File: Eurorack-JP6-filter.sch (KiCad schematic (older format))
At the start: 79 parts

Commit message: schematic capture almost finished
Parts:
- removed C?: C_US, symbol C_US
- removed R?: R_US, symbol R_US
- removed U?: LM13700, symbol LM13700
- removed U?: DG408, symbol DG408
- removed VR?: POT_US, symbol POT_US
- added C?: 33pF, symbol C_US
- added C? (x2): 330pF, symbol C_US
- added C?: 4.7pF, symbol C_US
- added C?: 22pF, symbol C_US
- added C? (x2): 10μF, symbol CP_US
- added C?: 0.47μ, symbol C_US
- added D? (x2): 1N914, symbol D
- added D? (x4): LED, symbol LED
- added J?: JACK_MONO_SW, symbol JACK_MONO_SW
- added P?: CONN_02X05, symbol CONN_02X05
- added Q? (x2): J112, symbol Q_NJFET_DGS
- added R? (x5): 100K, symbol R_US
- added R? (x3): 68K, symbol R_US
- added R? (x3): 560, symbol R_US
- added R? (x3): 18K, symbol R_US
- added R? (x4): 33K, symbol R_US
- added R? (x5): 10K, symbol R_US
- added R?: 47K, symbol R_US
- added R?: 1K, symbol R_US
- added R? (x2): 10, symbol R_US
- added SW?: TACT_SWITCH, symbol TACT_SWITCH
- added U? (x3): LM13700, symbol LM13700
- added U? (x2): TL072-, symbol TL072-
- added U?: 40106, symbol 40106
- added U?: DG409, symbol DG409
- added U? (x2): CD4027, symbol CD4027
- C?: value CP_US -> 10μF
- C?: value 47pF -> 4.7pF
- R?: value R_US -> 200K
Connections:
- net labels added: IN1, IN2, OUT2A, OUT2B, OUT4, SW1, SW2
- wire segments 139 -> 297
- no-connect marks 6 -> 15
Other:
- moved on the sheet: C?, J?, Q?, R?, U?, U?A, U?B, VR?

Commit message: schematic capture almost done. Power on Reset circuit breadboarded and implemented in schematic
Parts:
- removed U?: 40106, symbol 40106
- added C?: 0.47μ, symbol C_US
- added D?: 1N914, symbol D
- added J?: JACK_MONO_SW, symbol JACK_MONO_SW
- added R? (x2): 330, symbol R_US
- added R?: 33K, symbol R_US
- added R?: 100K, symbol R_US
- added U? (x6): CD40106, symbol CD40106
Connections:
- net +12V: now also D?.1 (K), R?.2, U?.14 (VDD)
- net GND: now also U?.13 (X), C?.2, J?.1, U?.11 (In), U?.13 (In), U?.5 (In), U?.7 (VSS), U?.9 (In); no longer U?.12 (Cd), U?.4 (Cd)
- net at R?.1, R?.1, R?.1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: now also R?.1
- net at C?.1, R?.1: now also R?.1, U?.1 (In); no longer SW?.1
- net at U?.3 (Cp): now also U?.2 (Out)
- new net: R?.2, SW?.1
- new net: U?.12 (Cd), U?.4 (Cd), U?.4 (Out)
- new net: C?.1, D?.2 (A), R?.1, R?.2
- new net: R?.1, U?.3 (In)
- new net: J?.3, R?.2
- no-connect marks 15 -> 19
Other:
- note added: "00 LOW PASS 24 dB\n01 LOW PASS 12 dB\n10 BAND PASS 12 dB\n11 HIGH PASS 24 dB"
- note added: "POWER ON RESET"
- note added: "SWITCH DEBOUNCE"
- moved on the sheet: C?, J?, Q?, R?, SW?, U?A, U?B, VR?

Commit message: capture done, still need to doublecheck and annotate, then do footprint association
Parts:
- added C? (x8): 100n, symbol C_US
- gave numbers to parts that had none: 7
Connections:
- net +12V: now also U4.8 (V+), U5.11 (V+), U6.11 (V+), U7.11 (V+), C?.1, C?.1, C?.1, C?.1
- net -12V: now also U4.4 (V-), U5.6 (V-), U6.6 (V-), U7.6 (V-), C?.2, C?.2, C?.2, C?.2
- net GND: now also U5.14 (+), U6.14 (+), U7.14 (+), C?.1, C?.1, C?.1, C?.1, C?.2, C?.2, C?.2, C?.2; no longer U5.3 (+), U6.3 (+), U7.3 (+)
- net at R?.1: now also U5.16; no longer U5.1
- net at R?.1, R?.2: now also U5.13 (-); no longer U5.4 (-)
- net at C?.1, Q?.2 (G): now also U5.12; no longer U5.5
- net at C?.2, R?.1, R?.2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: now also U6.12; no longer U6.5
- net at R?.1: now also U7.16; no longer U7.1
- net at R?.1, R?.2: now also U7.13 (-); no longer U7.4 (-)
- net at C?.1, Q?.2 (G): now also U7.12; no longer U7.5
- net at R?.1: now also U6.16; no longer U6.1
- net at R?.1, R?.2: now also U6.13 (-); no longer U6.4 (-)
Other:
- note added: "DECOUPLING"
- moved on the sheet: C?, R?

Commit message: annotation done, export netlist and start footprint assignment
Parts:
- added TP1, TP2: TEST_POINT, symbol TEST_POINT
- SW1: renamed from SW?; value TACT_SWITCH -> KS-01Q
- VR1, VR2, VR3, VR4, VR6: renamed from VR?; value POT_US -> 50K
- VR5: renamed from VR?; value POT_US -> 100K
- gave numbers to parts that had none: 122
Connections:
- net at Q2.1 (E1), Q2.4 (E2): now also R27.1
- net at Q2.5 (B2), R17.2, R23.2: now also R25.2, TP2.1
- net at Q1.1 (E1), Q1.4 (E2): now also R20.1
- net at Q1.5 (B2), R11.1, R12.1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: now also R15.1, TP1.1
- net IN1 renamed SUM1
- net IN2 renamed SUM2
- net SW1 renamed SWX1
- net SW2 renamed SWY2
- no-connect marks 19 -> 21
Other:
- note added: "GROUND UNUSED\nCMOS INPUTS"
- note added: "LOG"
- note added: "RESET FLIP FLOPS TO\n '00' ON POWER UP"
- moved on the sheet: U11C, U11D, U11E, U11F

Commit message: footprints assigned, about to start layout
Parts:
- removed Q3, Q4, Q5, Q6: J112, symbol Q_NJFET_DGS
- added Q3, Q4, Q5, Q6: J112, MyModules:SOT23-JRL, symbol Q_NJFET_SDG
- C1, C11, C12, C13, C14, C15, C16, C17, C18, C19, C2, C20, C21, C22, C25, C3, C4, C5, C6, C7, C8, C9: footprint (none) -> MyModules:SM0603-C-JRL
- C10, C23, C24, R19: footprint (none) -> MyModules:2MM-POL-CAP
- D1, D2, D3, D4: footprint (none) -> MyModules:3MM-LED
- D5, D6, D7: footprint (none) -> MyModules:SOD323-JRL
- J1, J2, J3, J4, J5, J6: footprint (none) -> MyModules:PJ-301B-JACK
- P1: footprint (none) -> Pin_Headers:Pin_Header_Straight_2x05
- Q1, Q2: footprint (none) -> synth:SOT363-JRL
- R1, R11, R12, R13, R14, R15, R16, R17, R18, R2, R20, R21, R22, R23, R24, R25, R26, R27, R28, R29, R3, R30, R31, R32, R33, R34, R35, R36, R37, R38, R39, R4, R40, R41, R42, R43, R44, R45, R46, R47, R48, R49, R5, R50, R51, R52, R53, R54, R55, R56, R57, R58, R59, R6, R60, R61, R62, R63, R64, R65, R66, R67, R68, R69, R7, R70, R71, R72, R8, R9: footprint (none) -> MyModules:SM0603-R-JRL
- R10: value R_US -> 680K; footprint (none) -> MyModules:SM0603-R-JRL
- SW1: footprint (none) -> synth:KS-01Q-02-JRL
- TP1, TP2: footprint (none) -> MyModules:TEST POINT
- U1, U2, U3, U4: footprint (none) -> MyModules:TSSOP8-JRL
- U10, U9: footprint (none) -> Housings_SSOP:TSSOP-16_4.4x5mm_Pitch0.65mm
- U11: footprint (none) -> Housings_SSOP:TSSOP-14_4.4x5mm_Pitch0.65mm
- U5, U6, U7, U8: footprint (none) -> synth:SO16-JRL
- VR1, VR2, VR3, VR4: footprint (none) -> synth:RV16A-41-JRL
- VR5, VR7: footprint (none) -> MyModules:Bourns_3362P
- VR6: footprint (none) -> synth:RD901F-ALPHA-POT
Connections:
- net +12V: now also Q3.2 (D), Q4.2 (D), Q5.2 (D), Q6.2 (D)
- net at C6.1, U5.5: now also Q3.3 (G)
- net at R33.2, R35.2, R37.2: now also Q3.1 (S)
- net at C7.1, U5.12: now also Q4.3 (G)
- net at C3.1, R24.2, R40.2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: now also Q4.1 (S)
- net at C18.1, U7.5: now also Q5.3 (G)
- net at R50.1, R57.2, R60.2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: now also Q5.1 (S)
- net at C25.1, U7.12: now also Q6.3 (G)
- net at C8.1, R45.2, R69.2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: now also Q6.1 (S)

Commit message: placing components, a few footprints updated
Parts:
- R66, R67: footprint MyModules:SM0603-R-JRL -> MyModules:SM0805-HAND
- VR6: footprint synth:RD901F-ALPHA-POT -> synth:RV16A-41-JRL
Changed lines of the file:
@@
 F 0 "VR6" H 2350 10600 50  0000 C CNN
 F 1 "50K" H 2350 10670 50  0000 C CNN
-F 2 "synth:RD901F-ALPHA-POT" H 2350 10750 60  0001 C CNN
+F 2 "synth:RV16A-41-JRL" H 2350 10750 60  0001 C CNN
 F 3 "" H 2350 10750 60  0000 C CNN
 	1    2350 10750
@@
 F 0 "R66" V 18680 1400 50  0000 C CNN
 F 1 "10" V 18520 1400 50  0000 C CNN
-F 2 "MyModules:SM0603-R-JRL" H 18600 1400 60  0001 C CNN
+F 2 "MyModules:SM0805-HAND" H 18600 1400 60  0001 C CNN
 F 3 "" H 18600 1400 60  0000 C CNN
 	1    18600 1400
@@
 F 0 "R67" V 18680 2300 50  0000 C CNN
 F 1 "10" V 18520 2300 50  0000 C CNN
-F 2 "MyModules:SM0603-R-JRL" H 18600 2300 60  0001 C CNN
+F 2 "MyModules:SM0805-HAND" H 18600 2300 60  0001 C CNN
 F 3 "" H 18600 2300 60  0000 C CNN
 	1    18600 2300

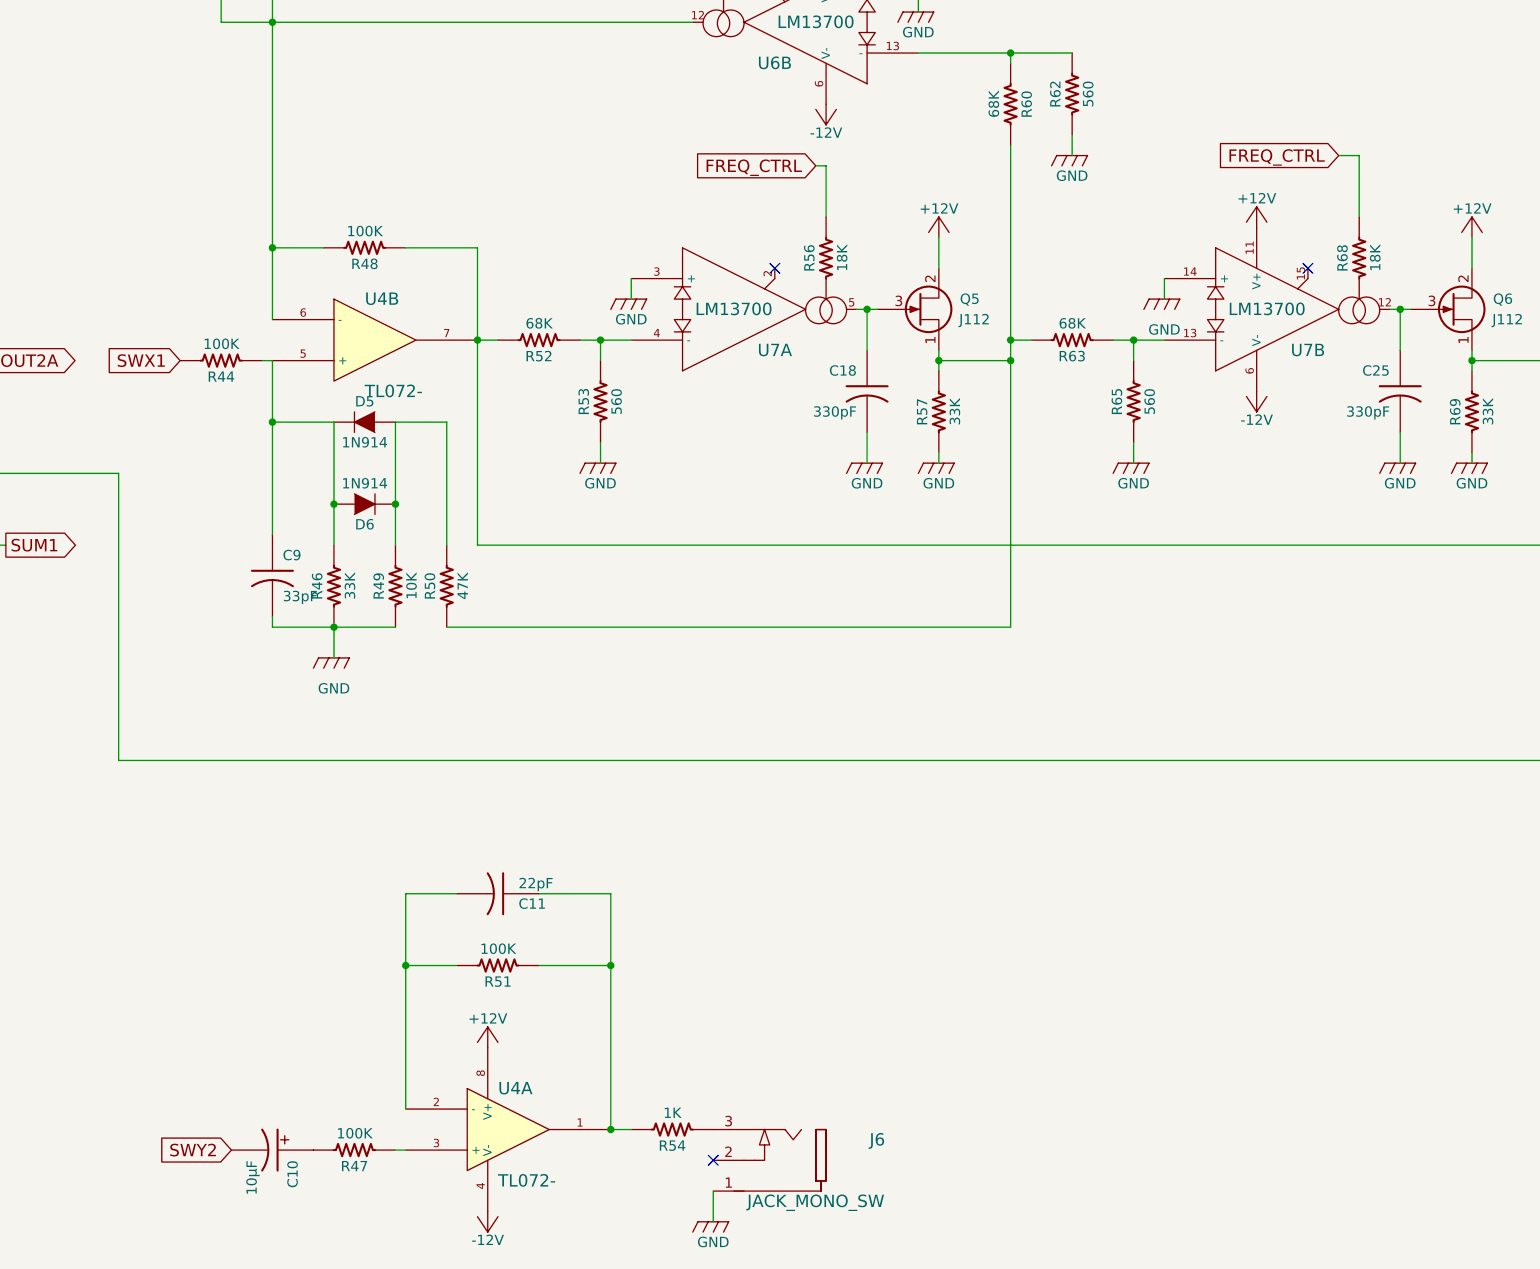
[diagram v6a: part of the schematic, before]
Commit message: components placed, beginning to route. current version crashes when 3D viewer is launched, going to try to open in previous version
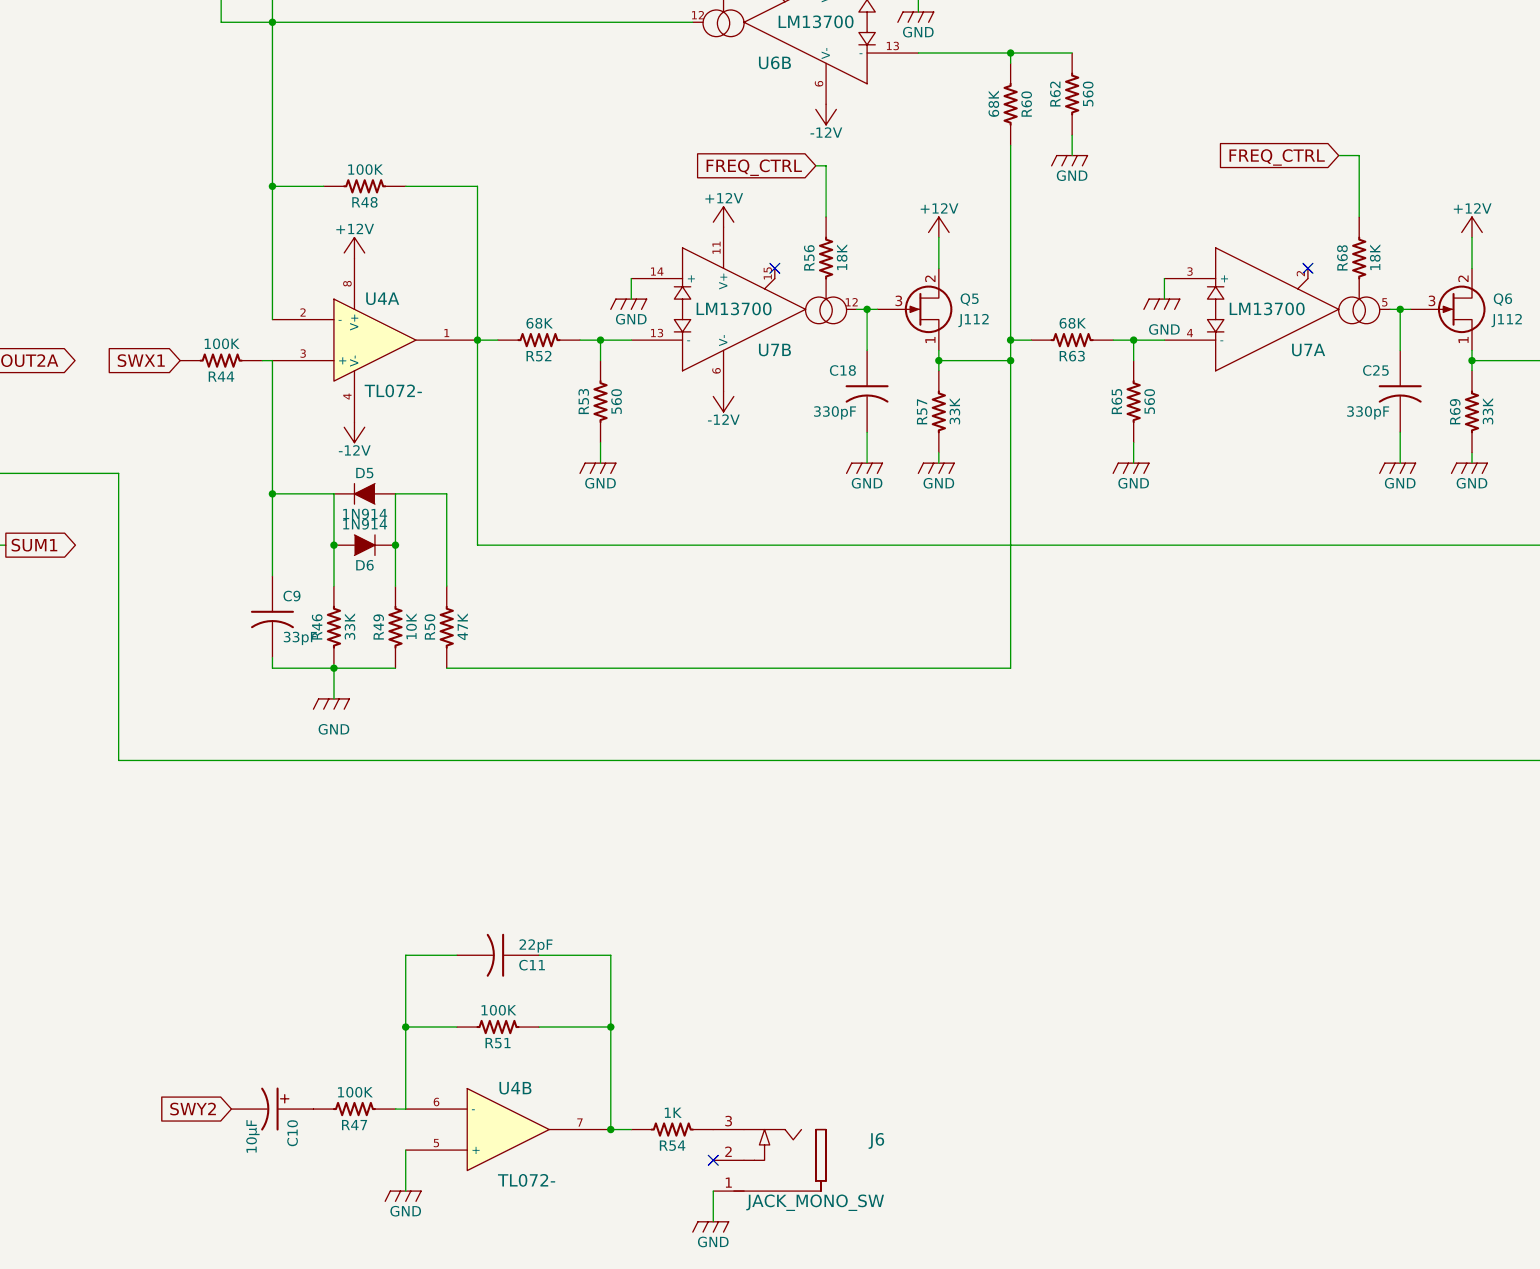
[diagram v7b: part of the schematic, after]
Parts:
- C18, C25, C6, C7: footprint MyModules:SM0603-C-JRL -> MyModules:CAP-BOX-PFR-5MM
- R19: footprint MyModules:2MM-POL-CAP -> MyModules:SM0805-HAND
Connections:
- net +12V: now also U4.8 (V+); no longer U4.8 (V+)
- net -12V: now also U4.4 (V-); no longer U4.4 (V-)
- net GND: now also U4.5 (+)
- net at U7.1: now also R68.1; no longer R56.1
- net at R52.1, R53.2: now also U7.13 (-); no longer U7.4 (-)
- net at C18.1, Q5.3 (G): now also U7.12; no longer U7.5
- net at C9.1, D5.1 (K), D6.2 (A)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: now also U4.3 (+); no longer U4.5 (+)
- net at C8.2, R45.1, R48.2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: now also U4.2 (-); no longer U4.6 (-)
- net at R48.1, R52.2, R71.2: now also U4.1; no longer U4.7
- net at C25.1, Q6.3 (G): now also U7.5; no longer U7.12
- net at R63.1, R65.2: now also U7.4 (-); no longer U7.13 (-)
- net at U7.16: now also R56.1; no longer R68.1
- net at C11.1, R51.1, R54.2: now also U4.7; no longer U4.1
- net at C11.2, R51.2: now also R47.1, U4.6 (-); no longer U4.2 (-)
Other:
- moved on the sheet: C10, C11, C9, D5, D6, R46, R47, R48, R49, R50, R51, U7A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
